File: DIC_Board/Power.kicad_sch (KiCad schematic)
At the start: 7 parts, among them J31 0430450200

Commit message: Wrapping up schematic
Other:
- moved on the sheet: C100, C101, D10, F10, J31, TP20, TP21

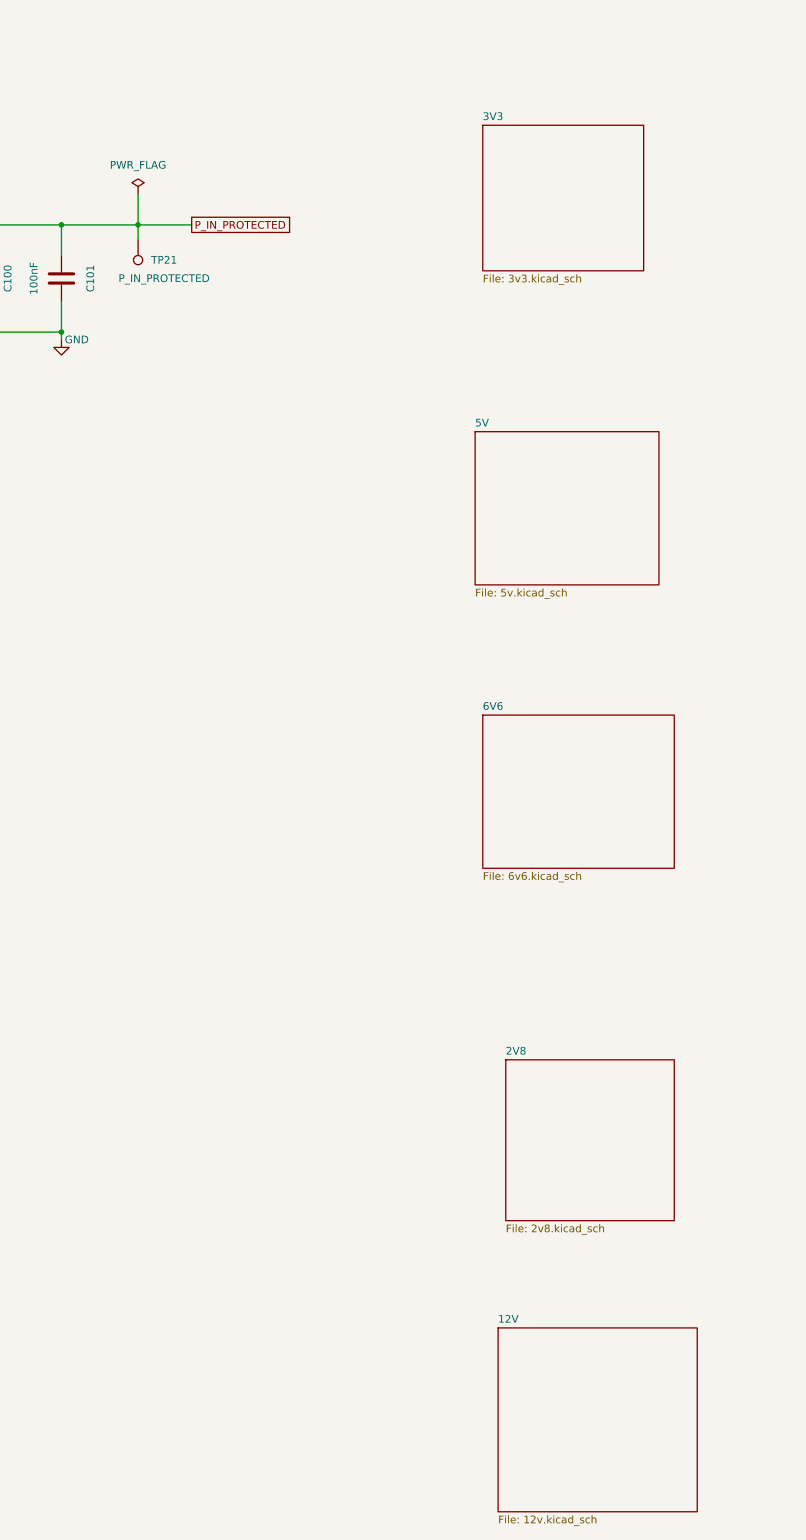
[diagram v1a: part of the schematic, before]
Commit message: Synchronize schematic hierarchy and MCU pin map
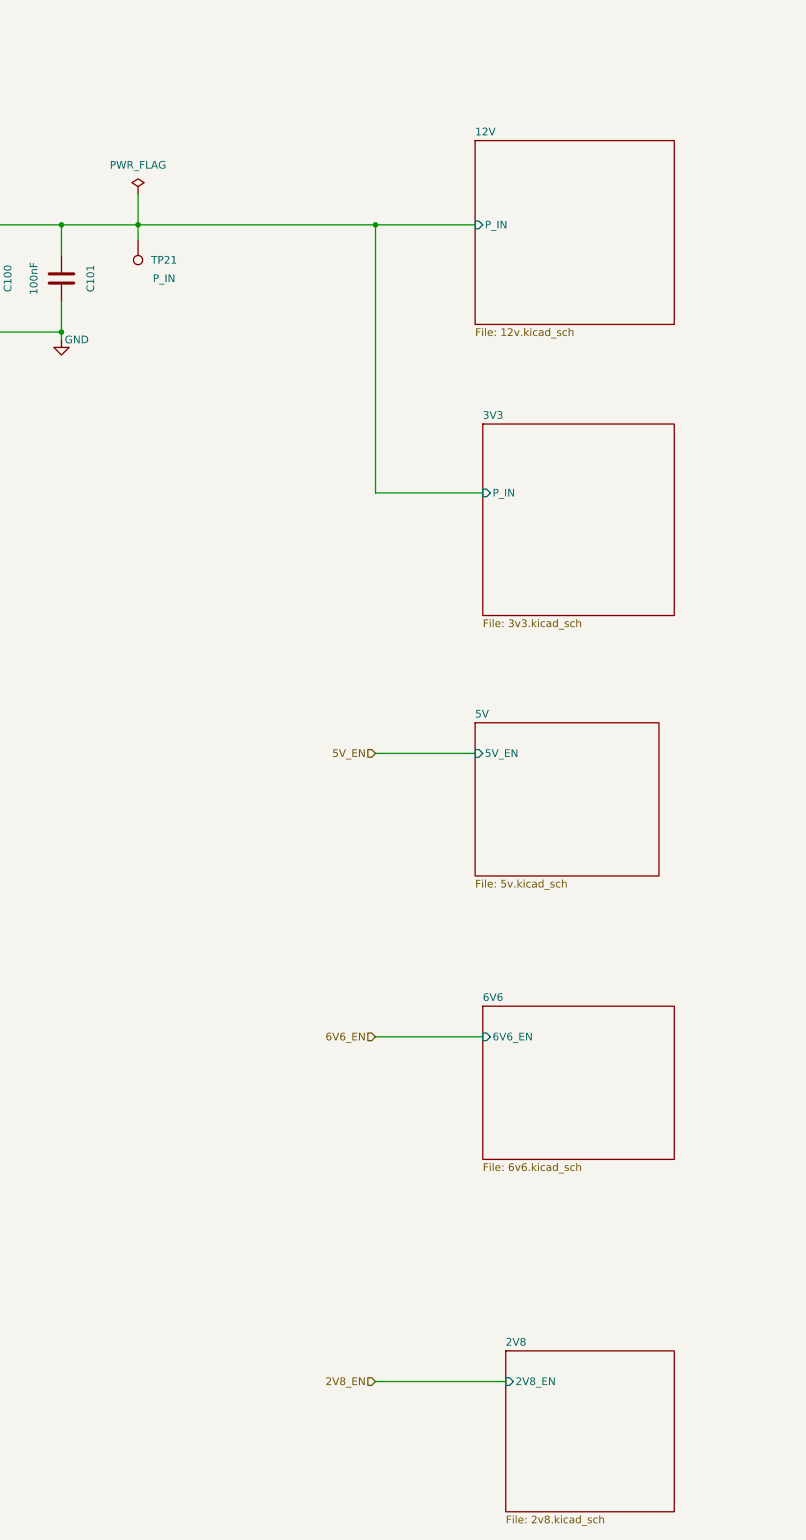
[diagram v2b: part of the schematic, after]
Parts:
- TP21: value P_IN_PROTECTED -> P_IN
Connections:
- net P_IN_PROTECTED renamed 12V/P_IN
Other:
- sheet 12V ports: added P_IN; removed none
- sheet 2V8 ports: added 2V8_EN; removed none
- sheet 3V3 ports: added P_IN; removed none
- sheet 5V ports: added 5V_EN; removed none
- sheet 6V6 ports: added 6V6_EN; removed none
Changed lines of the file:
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@@
+	)
+	(junction
+		(at 149.86 54.61)
+		(diameter 0)
+		(color 0 0 0 0)
 	)
 	(junction
@@
 	(wire
 		(pts
+			(xy 149.86 142.24) (xy 166.37 142.24)
+		)
+		(stroke
+			(width 0)
+			(type default)
+		)
+	)
+	(wire
+		(pts
+			(xy 149.86 189.23) (xy 167.64 189.23)
+		)
+		(stroke
+			(width 0)
+			(type default)
+		)
+	)
+	(wire
+		(pts
+			(xy 149.86 246.38) (xy 171.45 246.38)
+		)
+		(stroke
+			(width 0)
+			(type default)
+		)
+	)
+	(wire
+		(pts
 			(xy 58.42 54.61) (xy 58.42 55.88)
 		)
@@
 	(wire
 		(pts
+			(xy 149.86 54.61) (xy 149.86 99.06)
+		)
+		(stroke
+			(width 0)
+			(type default)
+		)
+	)
+	(wire
+		(pts
 			(xy 83.82 67.31) (xy 83.82 72.39)
 		)
@@
 	(wire
 		(pts
-			(xy 110.49 54.61) (xy 119.38 54.61)
+			(xy 110.49 54.61) (xy 166.37 54.61)
 		)
 		(stroke
@@
 	(wire
 		(pts
+			(xy 149.86 99.06) (xy 167.64 99.06)
+		)
+		(stroke
+			(width 0)
+			(type default)
+		)
+	)
+	(wire
+		(pts
 			(xy 59.69 72.39) (xy 71.12 72.39)
 		)
@@
 		)
 	)
-	(global_label "P_IN_PROTECTED"
-		(shape passive)
-		(at 119.38 54.61 0)
+	(hierarchical_label "5V_EN"
+		(shape input)
+		(at 149.86 142.24 180)
 		(effects
 			(font
 				(size 1.27 1.27)
 			)
-			(justify left)
-		)
-		(property "Intersheetrefs" "${INTERSHEET_REFS}"
-			(at 119.38 54.61 0)
-			(hide yes)
-			(show_name no)
-			(do_not_autoplace no)
-			(effects
-				(font
-					(size 1.27 1.27)
-				)
-			)
+			(justify right)
+		)
+	)
+	(hierarchical_label "6V6_EN"
+		(shape input)
+		(at 149.86 189.23 180)
+		(effects
+			(font
+				(size 1.27 1.27)
+			)
+			(justify right)
+		)
+	)
+	(hierarchical_label "2V8_EN"
+		(shape input)
+		(at 149.86 246.38 180)
+		(effects
+			(font
+				(size 1.27 1.27)
+			)
+			(justify right)
 		)
 	)
@@
 			)
 		)
-		(property "Value" "P_IN_PROTECTED"
+		(property "Value" "P_IN"
 			(at 114.808 63.5 0)
 			(show_name no)
@@
 	)
 	(sheet
-		(at 167.64 38.1)
-		(size 26.67 24.13)
+		(at 167.64 87.63)
+		(size 31.75 31.75)
 		(exclude_from_sim no)
 		(in_bom yes)
@@
 		)
 		(property "Sheetname" "3V3"
-			(at 167.64 37.3884 0)
+			(at 167.64 86.9184 0)
 			(show_name no)
 			(do_not_autoplace no)
@@
 		)
 		(property "Sheetfile" "3v3.kicad_sch"
-			(at 167.64 62.8146 0)
+			(at 167.64 119.9646 0)
 			(show_name no)
 			(do_not_autoplace no)
@@
 				)
 				(justify left top)
+			)
+		)
+		(pin "P_IN" input
+			(at 167.64 99.06 180)
+			(effects
+				(font
+					(size 1.27 1.27)
+				)
+				(justify left)
 			)
 		)
@@
 	)
 	(sheet
-		(at 167.64 135.89)
+		(at 167.64 184.15)
 		(size 31.75 25.4)
 		(exclude_from_sim no)
@@
 		)
 		(property "Sheetname" "6V6"
-			(at 167.64 135.1784 0)
+			(at 167.64 183.4384 0)
 			(show_name no)
 			(do_not_autoplace no)
@@
 		)
 		(property "Sheetfile" "6v6.kicad_sch"
-			(at 167.64 161.8746 0)
+			(at 167.64 210.1346 0)
 			(show_name no)
 			(do_not_autoplace no)
@@
 				)
 				(justify left top)
+			)
+		)
+		(pin "6V6_EN" input
+			(at 167.64 189.23 180)
+			(effects
+				(font
+					(size 1.27 1.27)
+				)
+				(justify left)
 			)
 		)
@@
 	)
 	(sheet
-		(at 170.18 237.49)
+		(at 166.37 40.64)
 		(size 33.02 30.48)
 		(exclude_from_sim no)
@@
 		)
 		(property "Sheetname" "12V"
-			(at 170.18 236.7784 0)
+			(at 166.37 39.9284 0)
 			(show_name no)
 			(do_not_autoplace no)
@@
 		)
 		(property "Sheetfile" "12v.kicad_sch"
-			(at 170.18 268.5546 0)
+			(at 166.37 71.7046 0)
 			(show_name no)
 			(do_not_autoplace no)
@@
 				)
 				(justify left top)
+			)
+		)
+		(pin "P_IN" input
+			(at 166.37 54.61 180)
+			(effects
+				(font
+					(size 1.27 1.27)
+				)
+				(justify left)
 			)
 		)
@@
 	)
 	(sheet
-		(at 171.45 193.04)
+		(at 171.45 241.3)
 		(size 27.94 26.67)
 		(exclude_from_sim no)
@@
 		)
 		(property "Sheetname" "2V8"
-			(at 171.45 192.3284 0)
+			(at 171.45 240.5884 0)
 			(show_name no)
 			(do_not_autoplace no)
@@
 		)
 		(property "Sheetfile" "2v8.kicad_sch"
-			(at 171.45 220.2946 0)
+			(at 171.45 268.5546 0)
 			(show_name no)
 			(do_not_autoplace no)
@@
 				)
 				(justify left top)
+			)
+		)
+		(pin "2V8_EN" input
+			(at 171.45 246.38 180)
+			(effects
+				(font
+					(size 1.27 1.27)
+				)
+				(justify left)
 			)
 		)
@@
 	)
 	(sheet
-		(at 166.37 88.9)
+		(at 166.37 137.16)
 		(size 30.48 25.4)
 		(exclude_from_sim no)
@@
 		)
 		(property "Sheetname" "5V"
-			(at 166.37 88.1884 0)
+			(at 166.37 136.4484 0)
 			(show_name no)
 			(do_not_autoplace no)
@@
 		)
 		(property "Sheetfile" "5v.kicad_sch"
-			(at 166.37 114.8846 0)
+			(at 166.37 163.1446 0)
 			(show_name no)
 			(do_not_autoplace no)
@@
 			)
 		)
+		(pin "5V_EN" input
+			(at 166.37 142.24 180)
+			(effects
+				(font
+					(size 1.27 1.27)
+				)
+				(justify left)
+			)
+		)

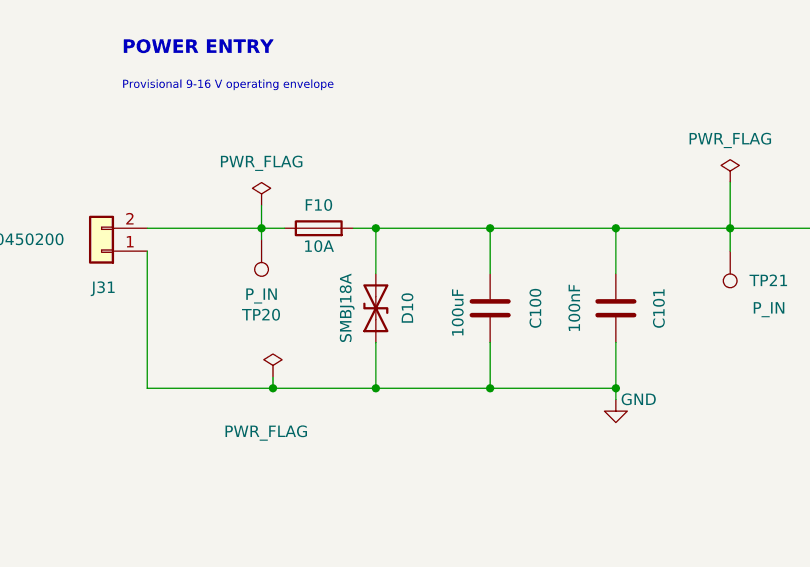
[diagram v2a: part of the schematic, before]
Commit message: Updated board for layout! All footprints added
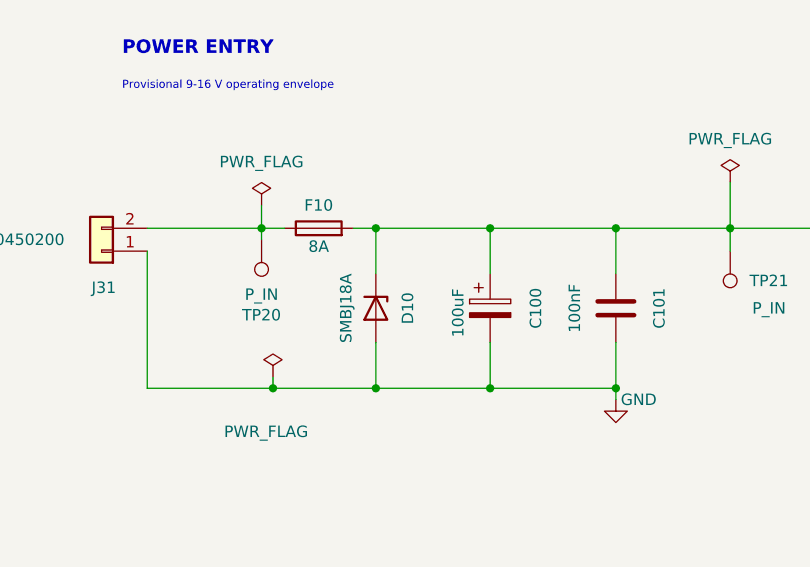
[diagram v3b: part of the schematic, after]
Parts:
- C100: symbol Device:C -> Device:C_Polarized
- D10: symbol Device:D_TVS -> Device:D_Zener; BOM Comments (none) -> SMBJ18A unidirectional: cathode band must face footprint pa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
- F10: value 10A -> 8A; BOM Source (none) -> Littelfuse 451/453 datasheet, revised 2025-12-01, 8A code 0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; Current Rating (none) -> 8A; MPN 0451010.MRL -> 0451008.MRL; Voltage Rating (none) -> 125VAC / 125VDC
- J31: BOM Comments Pin 1 = switched +12 V; pin 2 = GND. Mating housing 0430250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 -> Pin 1 = GND; pin 2 = external positive supply, through F10 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
- TP20, TP21: now left out of the parts list
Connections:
- net 12V/P_IN: now also D10.1 (K); no longer D10.2 (A2)
- net GND: now also D10.2 (A); no longer D10.1 (A1)
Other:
- moved on the sheet: D10
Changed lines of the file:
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@@
 			)
 		)
-		(property "BOM Comments" "Pin 1 = switched +12 V; pin 2 = GND. Mating housing 0430250200 and female contacts required."
+		(property "BOM Comments" "Pin 1 = GND; pin 2 = external positive supply, through F10 to P_IN. Mating housing 0430250200 and female contacts required. Verify harness polarity before connection."
 			(at 40.64 57.15 0)
 			(hide yes)
@@
 			)
 		)
-		(property "Value" "10A"
+		(property "Value" "8A"
 			(at 64.77 56.642 90)
 			(show_name no)
@@
 			)
 		)
-		(property "MPN" "0451010.MRL"
+		(property "MPN" "0451008.MRL"
 			(at 64.77 54.61 0)
 			(hide yes)
@@
 			)
 		)
+		(property "BOM Source" "Littelfuse 451/453 datasheet, revised 2025-12-01, 8A code 008.; same footprint as prior 10A part"
+			(at 0 0 0)
+			(hide yes)
+			(show_name no)
+			(do_not_autoplace no)
+			(effects
+				(font
+					(size 1.27 1.27)
+				)
+			)
+		)
+		(property "Current Rating" "8A"
+			(at 0 0 0)
+			(hide yes)
+			(show_name no)
+			(do_not_autoplace no)
+			(effects
+				(font
+					(size 1.27 1.27)
+				)
+			)
+		)
+		(property "Voltage Rating" "125VAC / 125VDC"
+			(at 0 0 0)
+			(hide yes)
+			(show_name no)
+			(do_not_autoplace no)
+			(effects
+				(font
+					(size 1.27 1.27)
+				)
+			)
+		)
 		(pin "1"
 		)
@@
 	)
 	(symbol
-		(lib_id "Device:C")
+		(lib_id "Device:C_Polarized")
 		(at 83.82 63.5 0)
 		(unit 1)
@@
 	)
 	(symbol
-		(lib_id "Device:D_TVS")
-		(at 71.12 63.5 90)
+		(lib_id "Device:D_Zener")
+		(at 71.12 63.5 270)
 		(unit 1)
 		(body_style 1)
@@
 			)
 		)
-		(property "Description" "Input TVS"
+		(property "Description" "Unidirectional input TVS; cathode pad 1 to P_IN, anode pad 2 to GND."
 			(at 71.12 63.5 0)
 			(hide yes)
@@
 			)
 		)
+		(property "BOM Comments" "SMBJ18A unidirectional: cathode band must face footprint pad 1/P_IN."
+			(at 0 0 0)
+			(hide yes)
+			(show_name no)
+			(do_not_autoplace no)
+			(effects
+				(font
+					(size 1.27 1.27)
+				)
+			)
+		)
 		(pin "1"
 		)
@@
 		(body_style 1)
 		(exclude_from_sim no)
-		(in_bom yes)
+		(in_bom no)
 		(on_board yes)
 		(in_pos_files yes)
@@
 		(body_style 1)
 		(exclude_from_sim no)
-		(in_bom yes)
-		(on_board yes)
-		(in_pos_files yes)
+		(in_bom no)
+		(on_board yes)
+		(in_pos_files yes)

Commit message: Let gpt6 astra have a go at routing. bad results.
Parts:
- TP20, TP21: footprint TestPoint:TestPoint_Plated_Hole_D2.0mm -> TestPoint:TestPoint_Pad_D1.0mm
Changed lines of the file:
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@@
 			)
 		)
-		(property "Footprint" "TestPoint:TestPoint_Plated_Hole_D2.0mm"
+		(property "Footprint" "TestPoint:TestPoint_Pad_D1.0mm"
 			(at 110.49 57.15 0)
 			(hide yes)
@@
 			)
 		)
-		(property "Footprint" "TestPoint:TestPoint_Plated_Hole_D2.0mm"
+		(property "Footprint" "TestPoint:TestPoint_Pad_D1.0mm"
 			(at 58.42 55.88 0)
 			(hide yes)
